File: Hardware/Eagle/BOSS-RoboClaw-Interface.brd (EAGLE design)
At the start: 41.6 x 48.3 mm, 9 parts, among them IC1 ISO7221ISO7221, J1 MOLEX 22112022, J2 MOLEX 22122034, J3 Amphenol 75869-130LF, J4 SAMTEC ESQ-105-44-G-S, J5 SAMTEC ESW-110-44-S-D, X1 Amphenol L77SDAH15SOL2RM8C309

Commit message: More layout changes
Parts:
- moved J1 5.24 mm to (29.2, 31.8)
- moved J2 5.08 mm to (39.4, 31.8)
- moved C1 2.54 mm to (23.5, 31.8)
- moved C2 2.54 mm to (12.1, 31.8)
- moved IC1 2.54 mm to (17.8, 31.8)
- moved J3 2.54 mm to (5.08, 31.8)
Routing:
- net M1A: track 9.95 -> 15.0 mm
- net M1B: track 13.8 -> 18.9 mm
- net LIMIT: track 31.0 -> 35.7 mm
- net VCC1: track 26.9 -> 29.6 mm
- net TX: track 29.6 -> 32.2 mm
- net RX: track 28.6 -> 31.1 mm
- net VCC2: track 15.1 -> 14.2 mm
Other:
- board size 41.6 x 48.3 mm -> 41.4 x 48.3 mm
- board text added: "2020-11-21 BOSS Motor Controller Interface"
- board text added: "ENC"
- board text added: "PI DB-15 Motor Connector Edge"
- board text removed: "2020-11-20 BOSS Motor Controller Interface"

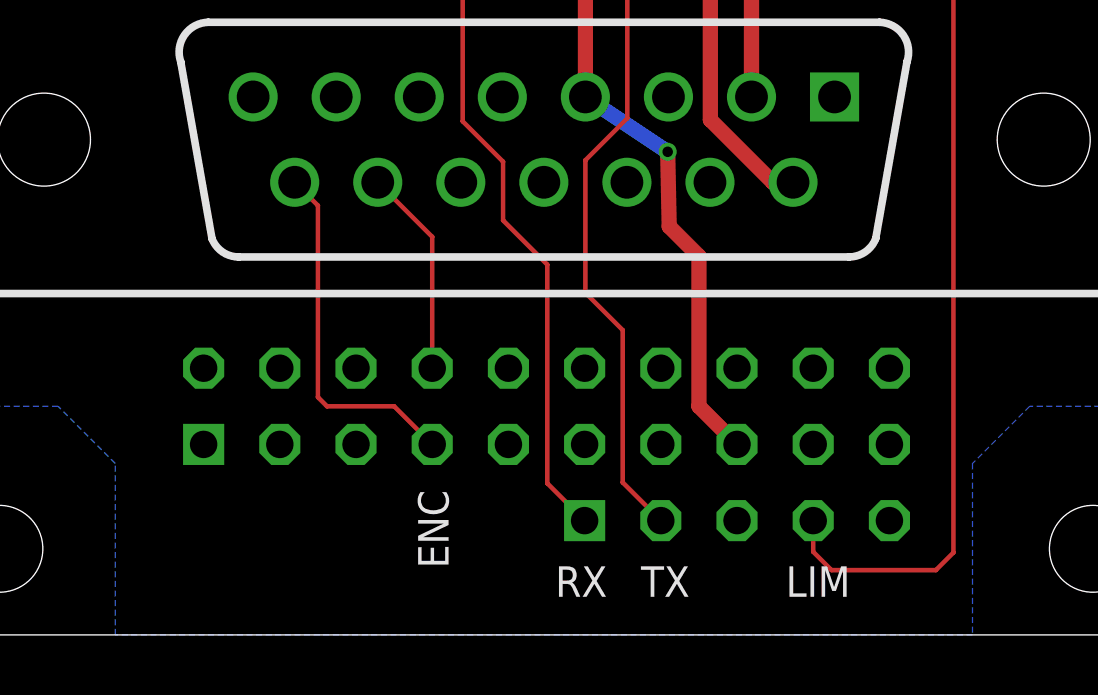
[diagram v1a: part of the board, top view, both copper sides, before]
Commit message: New headers for RoboClaw interface (need to check connections)
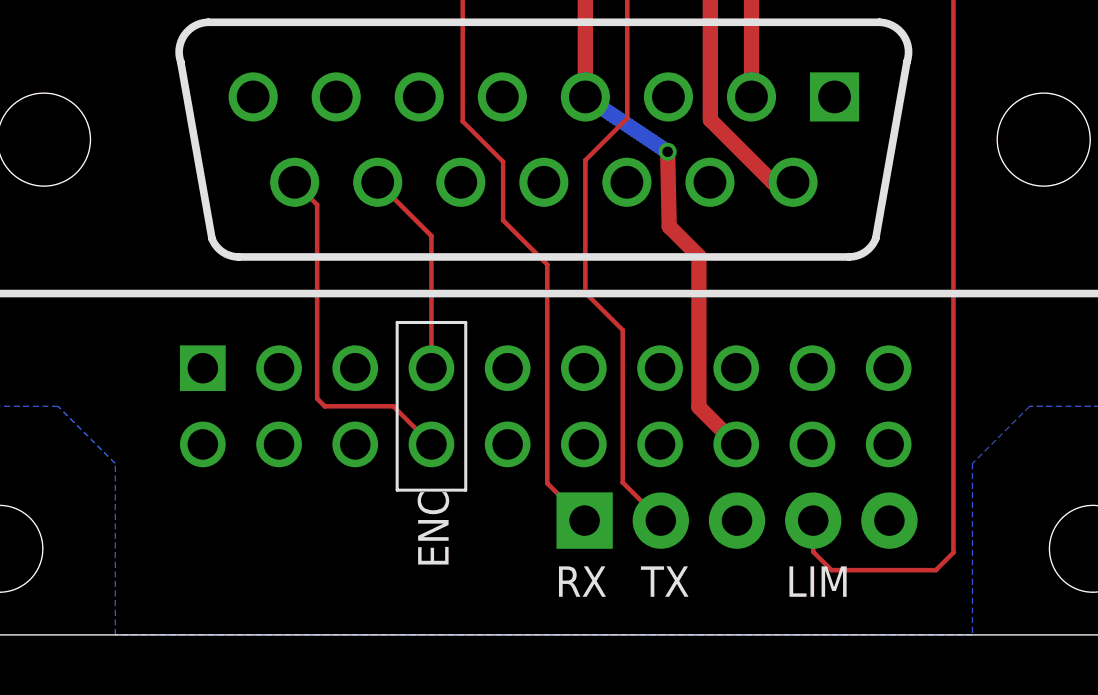
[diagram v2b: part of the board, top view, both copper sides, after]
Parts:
- removed J4: SAMTEC ESQ-105-44-G-S, AUmlib:FE05-1
- added J6: PINHD-1X5-ESQ-105-33-T-S, AUmlib:1X05-ESQ-105-33-T-S
- J5: value SAMTEC ESW-110-44-S-D -> (none); device AUmlib:FE10-2-SAMTEC-ESW-110-44-S-D -> AUmlib:2X10-ESQ-110-33-T-D
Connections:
- removed net ENC1A: J5.8, X1.14
- removed net ENC1B: J5.7, X1.15
- new net N$1: J5.8, X1.15
- new net N$2: J5.7, X1.14
- net GND: now also J5.15; no longer J5.16
- net LIMIT: now also J6.4; no longer J4.4
- net RX: now also J6.1; no longer J4.1
- net TX: now also J6.2; no longer J4.2
- net VCC1: now also J5.16; no longer J5.15
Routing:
- net N$1: track 0.00 -> 12.0 mm
- net ENC1B: track 11.9 -> 0.00 mm
- net ENC1A: track 6.95 -> 0.00 mm
- net N$2: track 0.00 -> 6.94 mm

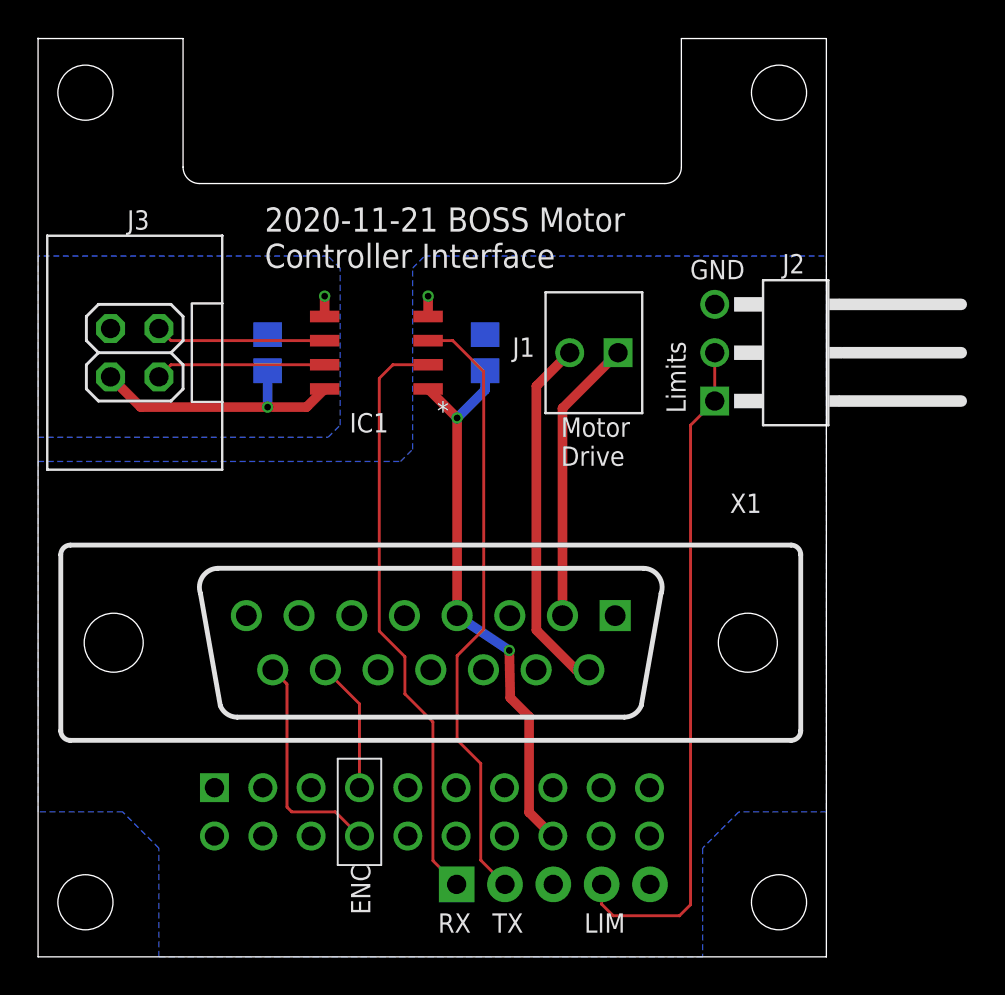
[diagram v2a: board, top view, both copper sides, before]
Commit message: Swapped ENC-A and ENC-B pins to be consistent
Also updated the board labels and changed the date to 2020-11-23.
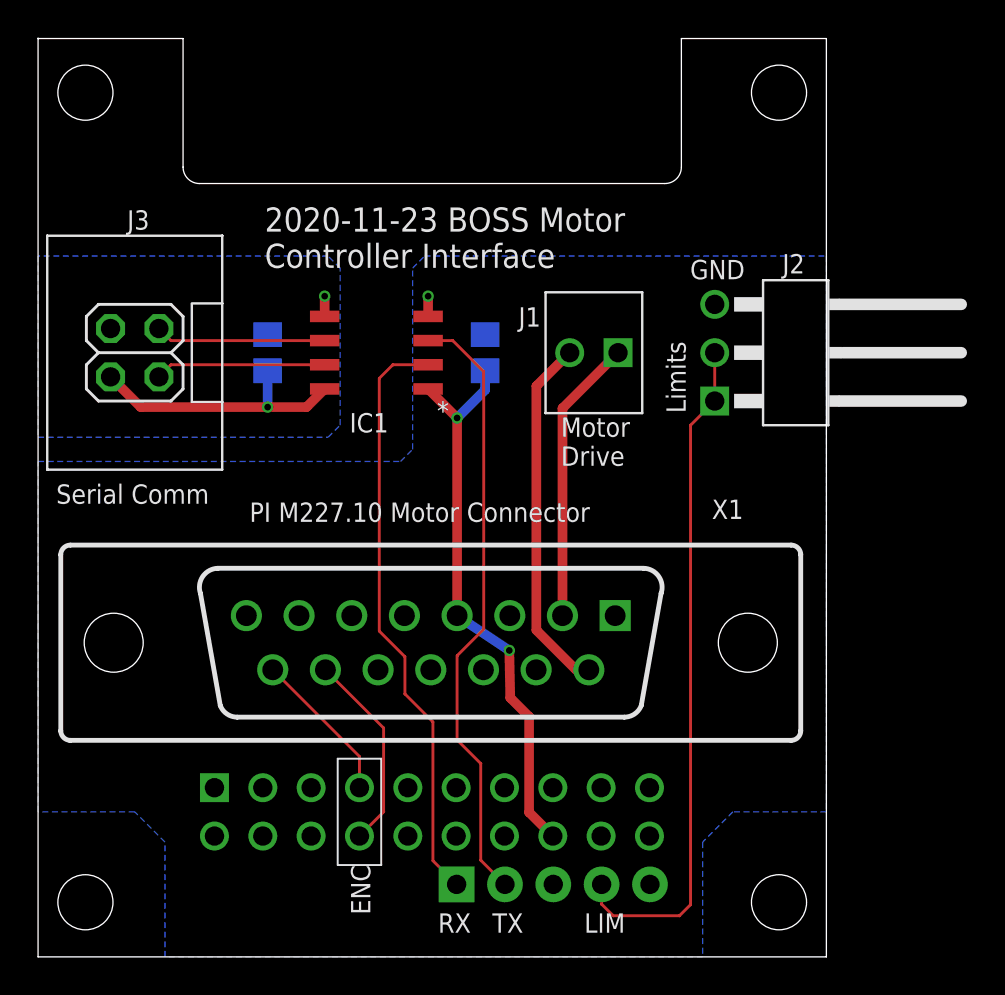
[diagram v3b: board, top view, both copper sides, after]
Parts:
- J5: value (none) -> SAMTEC ESQ-110-33-T-D
- J6: value PINHD-1X5-ESQ-105-33-T-S -> SAMTEC-ESQ-105-33-T-S
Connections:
- removed net N$1: J5.8, X1.15
- removed net N$2: J5.7, X1.14
- new net ENC1A: J5.8, X1.14
- new net ENC1B: J5.7, X1.15
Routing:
- net N$1: track 12.0 -> 0.00 mm
- net ENC1A: track 0.00 -> 10.5 mm
- net ENC1B: track 0.00 -> 8.09 mm
- net N$2: track 6.94 -> 0.00 mm
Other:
- board text added: "2020-11-23 BOSS Motor Controller Interface"
- board text added: "PI M227.10 Motor Connector"
- board text added: "Serial Comm"
- board text removed: "2020-11-21 BOSS Motor Controller Interface"
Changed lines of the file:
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@@
 <setting verticaltext="up"/>
 </settings>
-<grid distance="0.005" unitdist="inch" unit="inch" style="lines" multiple="1" display="yes" altdistance="5" altunitdist="mil" altunit="mil"/>
+<grid distance="0.0125" unitdist="inch" unit="inch" style="lines" multiple="1" display="yes" altdistance="5" altunitdist="mil" altunit="mil"/>
 <layers>
 <layer number="1" name="Top" color="4" fill="1" visible="yes" active="yes"/>
@@
 <layer number="49" name="Reference" color="7" fill="1" visible="yes" active="yes"/>
 <layer number="50" name="dxf" color="7" fill="1" visible="no" active="no"/>
-<layer number="51" name="tDocu" color="7" fill="1" visible="yes" active="yes"/>
+<layer number="51" name="tDocu" color="7" fill="1" visible="no" active="yes"/>
 <layer number="52" name="bDocu" color="7" fill="1" visible="yes" active="yes"/>
 <layer number="53" name="tGND_GNDA" color="7" fill="1" visible="no" active="no"/>
@@
 <board>
 <description>Basic Micro 2x7A RoboClaw interface to PI M-227.10 motor mikel.</description>
-<fusionsync huburn="a.cGVyc29uYWw6dWUyZDgyNjcx" projecturn="a.cGVyc29uYWw6dWUyZDgyNjcxIzIwMTgxMjIwMTY2NDc1MjMx" f3durn="urn:adsk.wipprod:dm.lineage:qemoZLx4Q2igI8rCdvDi4A" pcbguid="dc5b1513-d717-4bee-81ed-ee262294f200" lastpulledtime="" lastsyncedchangeguid="640551e2-8e01-6089-9af3-421ee07b5960" latestrevisionid="" lastsyncedrevisionid="" lastboardhashguid="8ddc0d05-a0c7-f717-4274-e7057d818ed3" lastpushedtime="2020-11-23T02:29:30Z" linktopcb3d="false"/>
+<fusionsync huburn="a.cGVyc29uYWw6dWUyZDgyNjcx" projecturn="a.cGVyc29uYWw6dWUyZDgyNjcxIzIwMTgxMjIwMTY2NDc1MjMx" f3durn="urn:adsk.wipprod:dm.lineage:qemoZLx4Q2igI8rCdvDi4A" pcbguid="dc5b1513-d717-4bee-81ed-ee262294f200" lastpulledtime="" lastsyncedchangeguid="640551e2-8e01-6089-9af3-421ee07b5960" latestrevisionid="" lastsyncedrevisionid="" lastboardhashguid="c83e0671-1a23-f1e2-1b8e-b8cdd854d6ba" lastpushedtime="2020-11-23T16:08:20Z" linktopcb3d="false"/>
 <plain>
 <wire x1="0" y1="0" x2="41.4274" y2="0" width="0" layer="20"/>
@@
 <wire x1="8.4836" y1="40.64" x2="32.9438" y2="40.64" width="0" layer="20"/>
 <wire x1="33.8074" y1="48.26" x2="41.4274" y2="48.26" width="0" layer="20"/>
-<text x="11.9126" y="36.2077" size="1.27" layer="21" font="vector">2020-11-21 BOSS Motor
+<text x="11.9126" y="36.2077" size="1.27" layer="21" font="vector">2020-11-23 BOSS Motor
 Controller Interface</text>
 <text x="34.036" y="28.575" size="1.016" layer="21" font="vector" rot="R90">Limits</text>
@@
 <wire x1="15.748" y1="10.414" x2="15.748" y2="4.826" width="0.1016" layer="21"/>
 <wire x1="15.748" y1="4.826" x2="18.034" y2="4.826" width="0.1016" layer="21"/>
+<text x="0.9525" y="23.8125" size="1.016" layer="21" font="vector">Serial Comm</text>
+<text x="11.1125" y="22.86" size="1.016" layer="21" font="vector">PI M227.10 Motor Connector</text>
 </plain>
 <attributes>
@@
 <attribute name="MF" value="" x="53.6575" y="10.16" size="1.778" layer="27" display="off"/>
 <attribute name="MPN" value="" x="53.6575" y="10.16" size="1.778" layer="27" display="off"/>
-<attribute name="NAME" x="36.3601" y="23.3299" size="1.016" layer="25"/>
+<attribute name="NAME" x="35.4076" y="23.0124" size="1.016" layer="25"/>
 <attribute name="OC_FARNELL" value="unknown" x="53.6575" y="10.16" size="1.778" layer="27" display="off"/>
 <attribute name="OC_NEWARK" value="unknown" x="53.6575" y="10.16" size="1.778" layer="27" display="off"/>
@@
 </element>
 <element name="J1" library="AUmlib" library_urn="urn:adsk.eagle:library:9166017" package="1X02-MOLEX-22112022" package3d_urn="urn:adsk.eagle:package:24727026/5" value="MOLEX 22112022" x="29.21" y="31.75" smashed="yes" rot="R180">
-<attribute name="NAME" x="26.0985" y="32.5501" size="1.016" layer="25" font="vector" rot="R180"/>
+<attribute name="NAME" x="26.416" y="34.1376" size="1.016" layer="25" font="vector" rot="R180"/>
 </element>
 <element name="J2" library="AUmlib" library_urn="urn:adsk.eagle:library:9166017" package="1X03RA-MOLEX-22122034" package3d_urn="urn:adsk.eagle:package:24728688/10" value="MOLEX 22122034" x="39.37" y="31.75" smashed="yes" rot="R90">
 <attribute name="NAME" x="40.2844" y="36.9316" size="1.016" layer="25" font="vector" rot="R180"/>
 </element>
-<element name="J6" library="AUmlib" library_urn="urn:adsk.eagle:library:9166017" package="1X05-ESQ-105-33-T-S" package3d_urn="urn:adsk.eagle:package:24929591/4" value="PINHD-1X5-ESQ-105-33-T-S" x="27.0764" y="3.81" smashed="yes" rot="MR180">
-<attribute name="NAME" x="25.8064" y="1.143" size="1.016" layer="26" font="vector" rot="MR180"/>
-<attribute name="VALUE" x="25.8064" y="7.112" size="1.016" layer="28" font="vector" rot="MR180"/>
-</element>
-<element name="J5" library="AUmlib" library_urn="urn:adsk.eagle:library:9166017" package="2X10-ESQ-110-33-T-D" package3d_urn="urn:adsk.eagle:package:24929474/2" value="" x="20.701" y="7.62" smashed="yes" rot="MR180">
-<attribute name="NAME" x="8.001" y="4.445" size="1.27" layer="26" ratio="10" rot="MR180"/>
-<attribute name="VALUE" x="8.001" y="12.065" size="1.27" layer="28" rot="MR180"/>
+<element name="J6" library="AUmlib" library_urn="urn:adsk.eagle:library:9166017" package="1X05-ESQ-105-33-T-S" package3d_urn="urn:adsk.eagle:package:24929591/4" value="SAMTEC-ESQ-105-33-T-S" x="27.0764" y="3.81" smashed="yes" rot="MR180">
+<attribute name="NAME" x="18.5039" y="4.0005" size="1.016" layer="26" font="vector" rot="MR180"/>
+</element>
+<element name="J5" library="AUmlib" library_urn="urn:adsk.eagle:library:9166017" package="2X10-ESQ-110-33-T-D" package3d_urn="urn:adsk.eagle:package:24929474/2" value="SAMTEC ESQ-110-33-T-D" x="20.701" y="7.62" smashed="yes" rot="MR180">
+<attribute name="NAME" x="5.7785" y="8.255" size="1.016" layer="26" rot="MR180"/>
 </element>
 </elements>
@@
 <signal name="GND">
 <contactref element="C1" pad="2"/>
-<contactref element="X1" pad="6"/>
 <contactref element="IC1" pad="4"/>
 <contactref element="J2" pad="3"/>
@@
 <vertex x="41.4274" y="36.83"/>
 <vertex x="41.4274" y="7.62"/>
-<vertex x="36.83" y="7.62"/>
-<vertex x="34.925" y="5.715"/>
+<vertex x="36.5125" y="7.62"/>
+<vertex x="34.925" y="6.0325"/>
 <vertex x="34.925" y="0"/>
-<vertex x="6.35" y="0"/>
-<vertex x="6.35" y="5.715"/>
-<vertex x="4.445" y="7.62"/>
+<vertex x="6.6675" y="0"/>
+<vertex x="6.6675" y="6.0325"/>
+<vertex x="5.08" y="7.62"/>
 <vertex x="0" y="7.62"/>
 <vertex x="0" y="26.035"/>
@@
 <via x="20.4978" y="34.7218" extent="1-16" drill="0.35"/>
 <wire x1="20.4978" y1="33.655" x2="20.4978" y2="34.7218" width="0.508" layer="1"/>
+<contactref element="X1" pad="6"/>
 <contactref element="J5" pad="15"/>
 </signal>
@@
 <contactref element="C1" pad="1"/>
 <contactref element="X1" pad="4"/>
-<contactref element="IC1" pad="1"/>
 <wire x1="24.8158" y1="13.6144" x2="25.8064" y2="12.6238" width="0.508" layer="1"/>
 <wire x1="24.8158" y1="13.6144" x2="24.765" y2="16.1036" width="0.508" layer="1"/>
@@
 <wire x1="22.0218" y1="17.9324" x2="22.0218" y2="28.321" width="0.508" layer="1"/>
 <via x="22.0218" y="28.321" extent="1-16" drill="0.35"/>
-<wire x1="20.4978" y1="29.845" x2="22.0218" y2="28.321" width="0.508" layer="1"/>
 <wire x1="23.495" y1="30.8" x2="23.495" y2="29.7942" width="0.508" layer="16"/>
 <wire x1="23.495" y1="29.7942" x2="22.0218" y2="28.321" width="0.508" layer="16"/>
@@
 <wire x1="25.8064" y1="7.5946" x2="27.051" y2="6.35" width="0.508" layer="1"/>
 <wire x1="25.8064" y1="12.6238" x2="25.8064" y2="7.5946" width="0.508" layer="1"/>
+<contactref element="IC1" pad="1"/>
+<wire x1="20.4978" y1="29.845" x2="22.0218" y2="28.321" width="0.508" layer="1"/>
 </signal>
 <signal name="GND-ISO">
@@
 <wire x1="26.1874" y1="29.9974" x2="27.94" y2="31.75" width="0.508" layer="1"/>
 </signal>
-<signal name="N$1">
+<signal name="ENC1A">
+<contactref element="J5" pad="8"/>
+<contactref element="X1" pad="14"/>
+<wire x1="15.1003" y1="15.0876" x2="18.161" y2="12.0269" width="0.1524" layer="1"/>
+<wire x1="18.161" y1="7.62" x2="16.891" y2="6.35" width="0.1524" layer="1"/>
+<wire x1="18.161" y1="12.0269" x2="18.161" y2="7.62" width="0.1524" layer="1"/>
+</signal>
+<signal name="ENC1B">
+<contactref element="J5" pad="7"/>
 <contactref element="X1" pad="15"/>
-<contactref element="J5" pad="8"/>
-<wire x1="12.3317" y1="15.0876" x2="13.081" y2="14.3383" width="0.1524" layer="1"/>
-<wire x1="13.081" y1="7.874" x2="13.335" y2="7.62" width="0.1524" layer="1"/>
-<wire x1="13.335" y1="7.62" x2="15.621" y2="7.62" width="0.1524" layer="1"/>
-<wire x1="15.621" y1="7.62" x2="16.891" y2="6.35" width="0.1524" layer="1"/>
-<wire x1="13.081" y1="14.3383" x2="13.081" y2="7.874" width="0.1524" layer="1"/>
-</signal>
-<signal name="N$2">
-<contactref element="J5" pad="7"/>
-<contactref element="X1" pad="14"/>
-<wire x1="15.1003" y1="15.0876" x2="16.891" y2="13.2969" width="0.1524" layer="1"/>
-<wire x1="16.891" y1="13.2969" x2="16.891" y2="8.89" width="0.1524" layer="1"/>
+<wire x1="12.3317" y1="15.0876" x2="16.891" y2="10.5283" width="0.1524" layer="1"/>
+<wire x1="16.891" y1="10.5283" x2="16.891" y2="8.89" width="0.1524" layer="1"/>
 </signal>
 </signals>

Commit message: No changes made; just saved new version
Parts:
- IC1: value ISO7221ISO7221 -> TI ISO7221ADR
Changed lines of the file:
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@@
 <board>
 <description>Basic Micro 2x7A RoboClaw interface to PI M-227.10 motor mikel.</description>
-<fusionsync huburn="a.cGVyc29uYWw6dWUyZDgyNjcx" projecturn="a.cGVyc29uYWw6dWUyZDgyNjcxIzIwMTgxMjIwMTY2NDc1MjMx" f3durn="urn:adsk.wipprod:dm.lineage:qemoZLx4Q2igI8rCdvDi4A" pcbguid="dc5b1513-d717-4bee-81ed-ee262294f200" lastpulledtime="" lastsyncedchangeguid="640551e2-8e01-6089-9af3-421ee07b5960" latestrevisionid="" lastsyncedrevisionid="" lastboardhashguid="c83e0671-1a23-f1e2-1b8e-b8cdd854d6ba" lastpushedtime="2020-11-23T16:08:20Z" linktopcb3d="false"/>
+<fusionsync huburn="a.cGVyc29uYWw6dWUyZDgyNjcx" projecturn="a.cGVyc29uYWw6dWUyZDgyNjcxIzIwMTgxMjIwMTY2NDc1MjMx" f3durn="urn:adsk.wipprod:dm.lineage:qemoZLx4Q2igI8rCdvDi4A" pcbguid="dc5b1513-d717-4bee-81ed-ee262294f200" lastpulledtime="" lastsyncedchangeguid="640551e2-8e01-6089-9af3-421ee07b5960" latestrevisionid="" lastsyncedrevisionid="" lastboardhashguid="5ea78dc1-fa9a-b686-c250-1ae1f5f38843" lastpushedtime="2020-11-23T17:20:39Z" linktopcb3d="false"/>
 <plain>
 <wire x1="0" y1="0" x2="41.4274" y2="0" width="0" layer="20"/>
@@
 <attribute name="SPICEPREFIX" value="C" x="12.065" y="31.75" size="1.778" layer="28" rot="MR90" display="off"/>
 </element>
-<element name="IC1" library="AUmlib" library_urn="urn:adsk.eagle:library:9166017" package="SO-08-ISO7221" package3d_urn="urn:adsk.eagle:package:24898359/3" value="ISO7221ISO7221" x="17.78" y="31.75" smashed="yes" rot="R180">
+<element name="IC1" library="AUmlib" library_urn="urn:adsk.eagle:library:9166017" package="SO-08-ISO7221" package3d_urn="urn:adsk.eagle:package:24898359/3" value="TI ISO7221ADR" x="17.78" y="31.75" smashed="yes" rot="R180">
 <attribute name="NAME" x="18.415" y="28.575" size="1.016" layer="25" font="vector" rot="R180"/>
 </element>

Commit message: Changed isolator chip to ISO7221AQDRQ1 from ISO7221ADR (better stock)
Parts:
- IC1: value TI ISO7221ADR -> ISO7221AQDRQ1
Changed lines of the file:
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@@
 <attribute name="SPICEPREFIX" value="C" x="12.065" y="31.75" size="1.778" layer="28" rot="MR90" display="off"/>
 </element>
-<element name="IC1" library="AUmlib" library_urn="urn:adsk.eagle:library:9166017" package="SO-08-ISO7221" package3d_urn="urn:adsk.eagle:package:24898359/3" value="TI ISO7221ADR" x="17.78" y="31.75" smashed="yes" rot="R180">
+<element name="IC1" library="AUmlib" library_urn="urn:adsk.eagle:library:9166017" package="SO-08-ISO7221" package3d_urn="urn:adsk.eagle:package:24898359/3" value="ISO7221AQDRQ1" x="17.78" y="31.75" smashed="yes" rot="R180">
 <attribute name="NAME" x="18.415" y="28.575" size="1.016" layer="25" font="vector" rot="R180"/>
 </element>
